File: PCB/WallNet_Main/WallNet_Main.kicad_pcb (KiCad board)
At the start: 4 copper layers, 121.7 x 158.2 mm, 87 parts, among them J1 Conn_01x05_Pin, J101 USB_C_Receptacle_PowerOnly_6P, J102 01x04 Molex, J201 01x04 Molex, J202 Conn_01x07_Socket, J203 02x12 Connector, Q201 BSS138, SW1 SW, U1 BT832, U101 BQ25895RTWT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

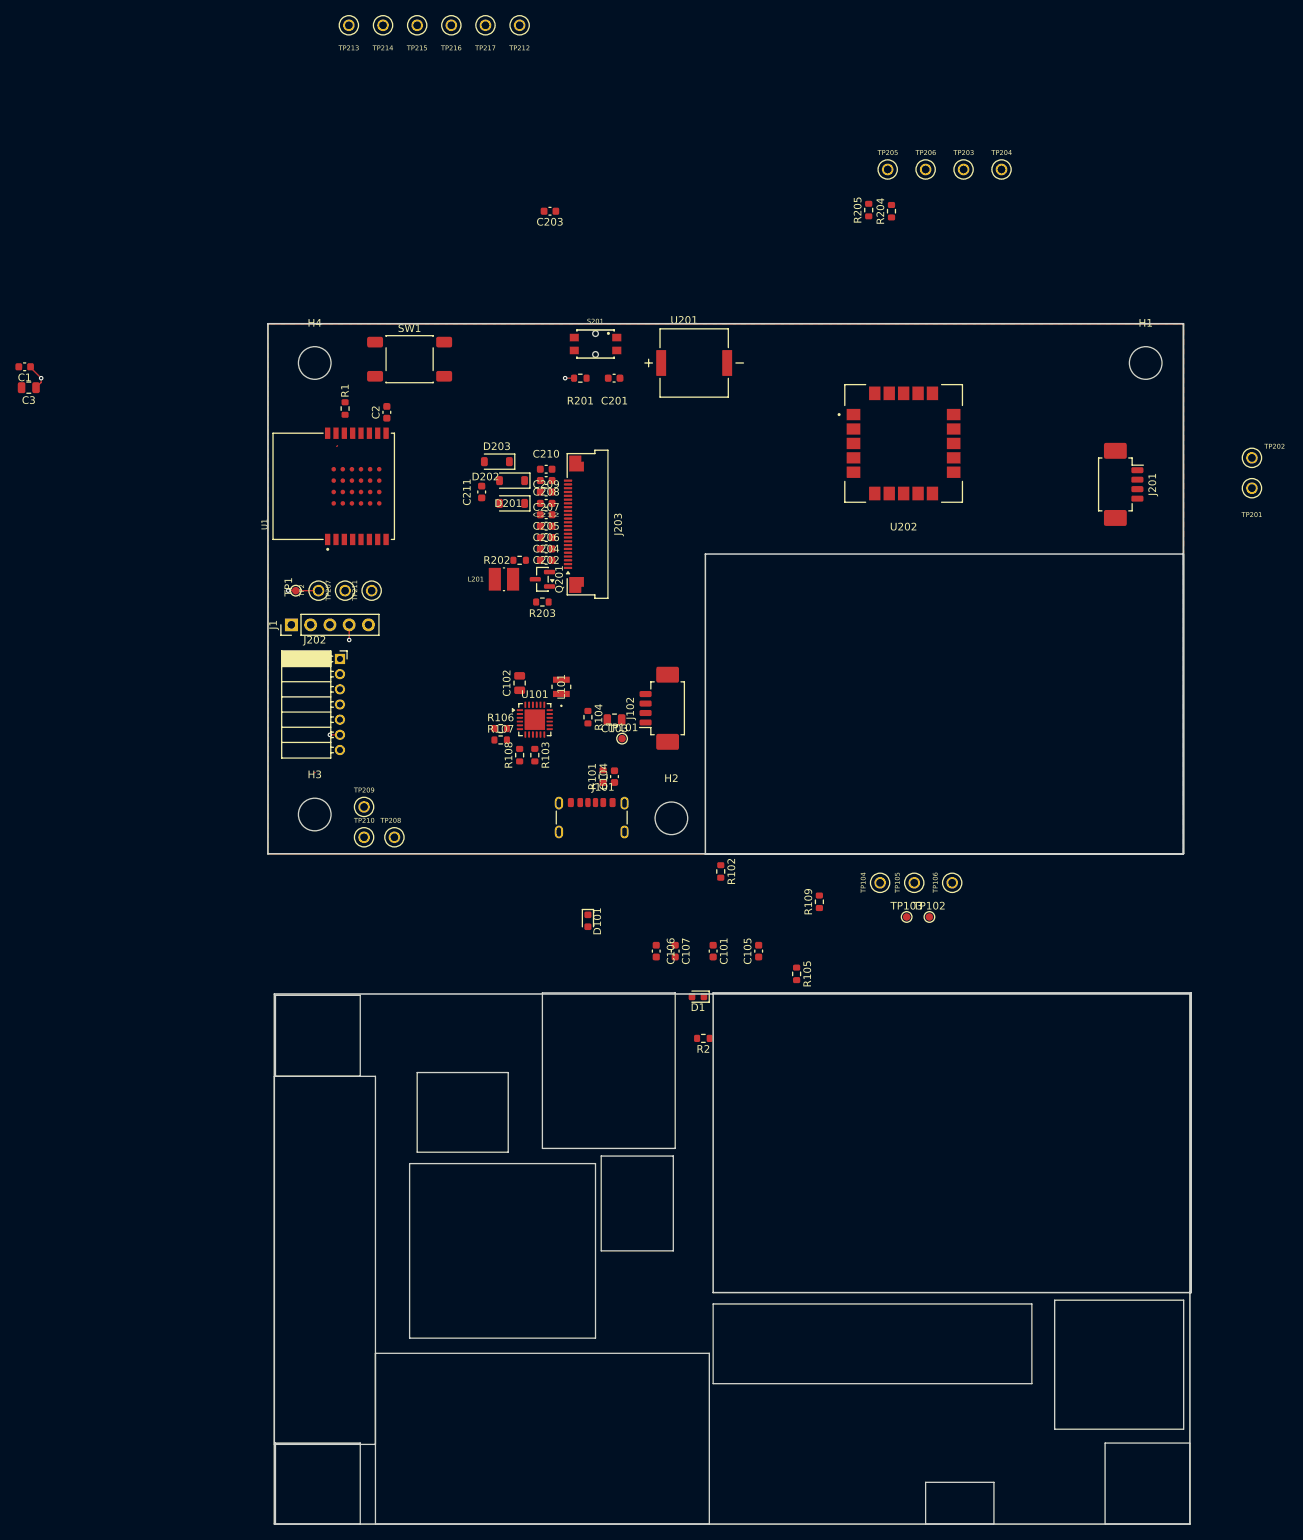
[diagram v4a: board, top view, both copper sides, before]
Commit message: Finished adding cutout, via, and mount hole for RFID
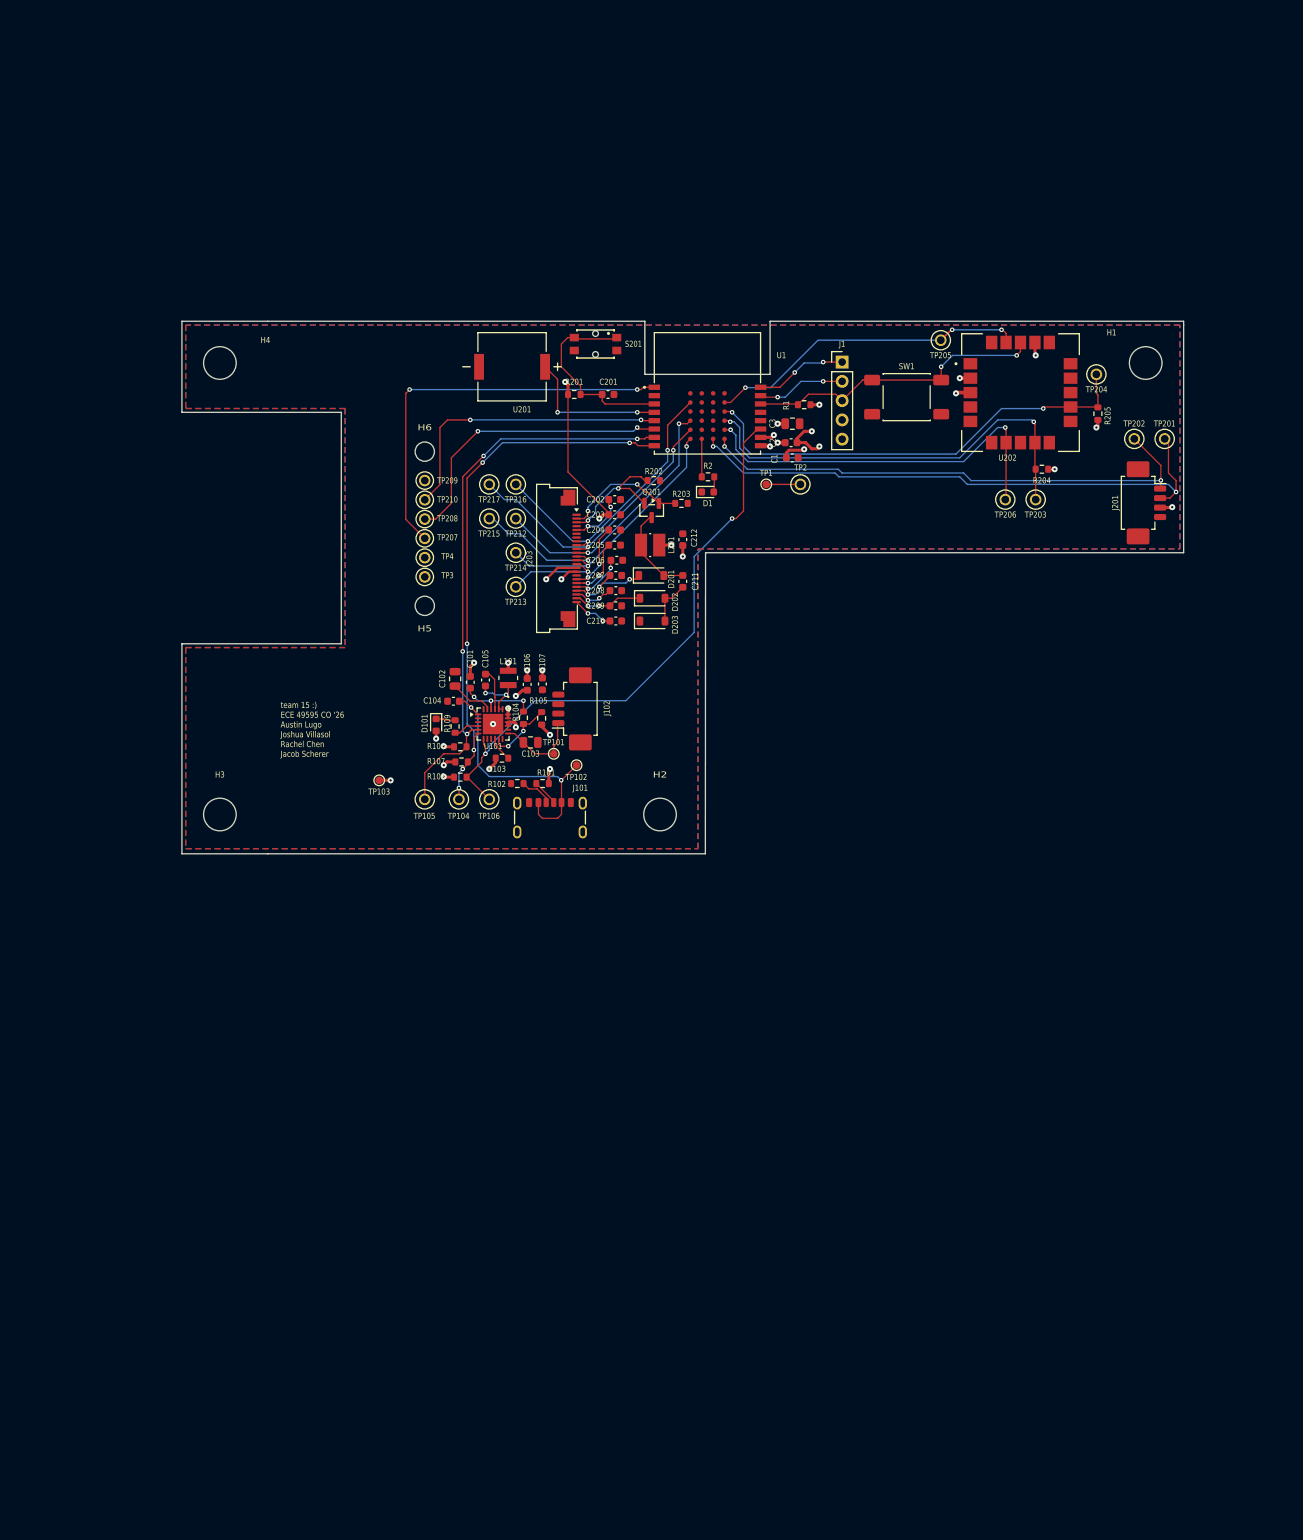
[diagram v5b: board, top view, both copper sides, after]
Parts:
- removed J202: Conn_01x07_Socket, Connector_PinSocket_2.00mm:PinSocket_1x07_P2.00mm_Horizontal
- removed TP211: RFID_SS, 5001:KEYSTONE_5001
- added H5: RFID_mount_1, MountingHole:MountingHole_4.3mm_M4, F.Cu at (32.0, 49.0)
- added H6: RFID_mount_2, MountingHole:MountingHole_4.3mm_M4, F.Cu at (32.0, 28.7)
- added TP3: RFID_VDD, 5001:KEYSTONE_5001, F.Cu at (32.0, 45.2)
- added TP4: RFID_GND, 5001:KEYSTONE_5001, F.Cu at (32.0, 42.6)
- TP207: value RFID_RST -> RFID_SCL
- TP208: value RFID_SCK -> RFID_SDA
- TP209: value RFID_MISO -> RFID_VEH
- TP210: value RFID_MOSI -> RFID_GPO
- moved C1 101.9 mm to (80.4, 29.5), turned to 0 degrees
- moved C3 100.7 mm to (80.5, 25.0), turned to 0 degrees
- moved J1 80.4 mm to (87.0, 16.9), turned to 0 degrees
- moved TP213 77.2 mm to (44.0, 46.5)
- moved R2 74.0 mm to (69.3, 32.0), turned to 0 degrees
- moved TP103 71.8 mm to (26.0, 72.0)
- moved TP214 71.7 mm to (44.0, 42.0)
- moved D1 66.5 mm to (69.3, 34.0), turned to 0 degrees
- moved SW1 65.7 mm to (95.5, 21.5)
- moved TP215 65.7 mm to (40.5, 37.5)
- moved TP105 65.4 mm to (32.0, 74.5), turned to 180 degrees
- moved TP2 65.0 mm to (81.5, 33.0), turned to 0 degrees
- moved TP212 65.0 mm to (44.0, 37.5)
- moved TP1 63.6 mm to (77.0, 33.0), turned to 0 degrees
- moved TP106 62.0 mm to (40.5, 74.5), turned to 180 degrees
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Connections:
- TP207 pad 1: /P18 -> /P26
- TP208 pad 1: /P20 -> /P03
- TP209 pad 1: /P02 -> /Sensors/RFID_VEH
- TP210 pad 1: /P03 -> /P02
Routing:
- net /P13: track 0.00 -> 76.1 mm, vias 0 -> 2
- net /P09: track 0.00 -> 76.0 mm, vias 0 -> 4
- net /P12: track 0.00 -> 74.5 mm, vias 0 -> 2
- net /P10: track 0.00 -> 72.7 mm, vias 0 -> 6
- net /P11: track 0.00 -> 68.9 mm, vias 0 -> 2
- net /P19: track 0.00 -> 60.3 mm, vias 0 -> 2
- net /P16: track 0.00 -> 56.4 mm, vias 0 -> 2
- net /P26: track 0.00 -> 53.2 mm, vias 0 -> 2
- net VDD_nrf: track 9.18 -> 60.4 mm, vias 4 -> 26
- net /P14: track 0.00 -> 50.8 mm, vias 0 -> 2
- net /P23: track 0.00 -> 44.6 mm, vias 0 -> 3
- net RESET: track 0.00 -> 40.2 mm, vias 0 -> 2
- net /P05: track 0.00 -> 39.1 mm, vias 0 -> 2
- net /P02: track 0.00 -> 39.1 mm, vias 0 -> 2
- net /P03: track 0.00 -> 38.8 mm, vias 0 -> 2
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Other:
- board size 121.7 x 158.2 mm -> 132 x 70.2 mm
- board text added: "team 15 :) ECE 49595 CO '26 Austin Lugo Joshua Villasol Rachel Chen Jacob Scherer"
- board text removed: "BQ + Components"
- board text removed: "Battery"
- board text removed: "Button"
- board text removed: "Buzzer"
- board text removed: "EINK + components"
- board text removed: "FingerPrint Molex + USBC"
- board text removed: "GPS"
- board text removed: "MH"
- board text removed: "Microcontroller"
- board text removed: "Molex Batt"
- board text removed: "RFID TEMPORARY"
